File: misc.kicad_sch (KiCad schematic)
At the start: 125 parts, among them CN2 Expansion, CN3 Cartridge, CN5 1P, CN504 AV Out, CN6 1P, IC401 74ACT241, IC513 MC34063AM, IC514 L7805, IC701 PIC16F630/18324, IC901 TL974, J1 Barrel_Jack, J2 EXT, Q1 MMBT3904, U1 TPS564257DRLR, U4 L7805

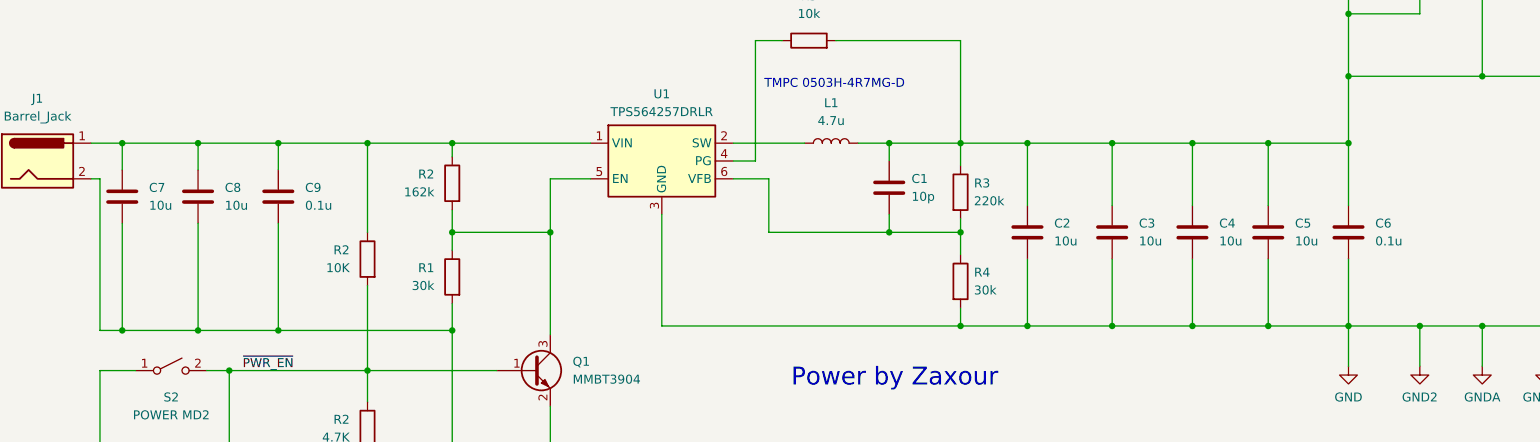
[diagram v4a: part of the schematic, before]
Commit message: BOM/footprint tweaks/corrections.
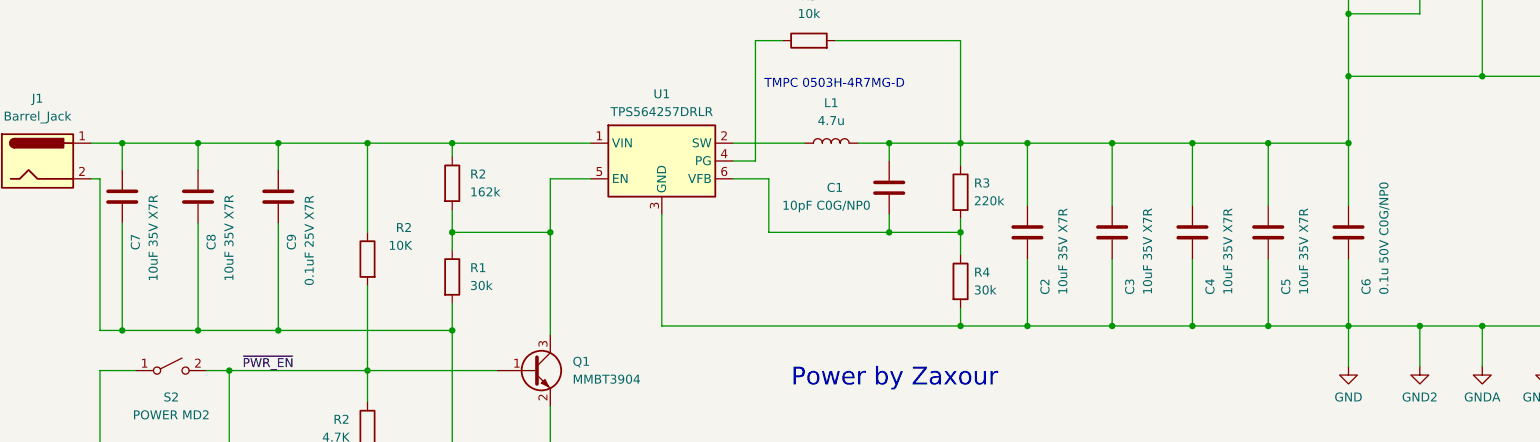
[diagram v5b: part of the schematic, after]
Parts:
- C1: value 10p -> 10pF C0G/NP0
- C2, C3, C4, C5, C7, C8: value 10u -> 10uF 35V X7R
- C6: value 0.1u -> 0.1u 50V C0G/NP0
- C9: value 0.1u -> 0.1uF 25V X7R
- R3, R4, R5: footprint Capacitor_SMD:C_0805_2012Metric -> Resistor_SMD:R_0805_2012Metric
- U1: footprint Package_TO_SOT_SMD:SOT-23-6 -> Neptune:SOT-563
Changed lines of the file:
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@@
       (effects (font (size 1.27 1.27)) (justify left))
     )
-    (property "Footprint" "Capacitor_SMD:C_0805_2012Metric" (at 154.432 227.33 90)
+    (property "Footprint" "Resistor_SMD:R_0805_2012Metric" (at 154.432 227.33 90)
       (effects (font (size 1.27 1.27)) hide)
     )
@@
       (effects (font (size 1.27 1.27)))
     )
-    (property "Footprint" "Package_TO_SOT_SMD:SOT-23-6" (at 114.935 229.235 0)
+    (property "Footprint" "Neptune:SOT-563" (at 114.935 229.235 0)
       (effects (font (size 1.27 1.27)) (justify left) hide)
     )
@@
   )
   (symbol (lib_id "Device:C") (at 146.05 226.695 0) (unit 1)
-    (in_bom yes) (on_board yes) (dnp no) (fields_autoplaced)
-    (property "Reference" "C1" (at 149.225 225.425 0)
+    (in_bom yes) (on_board yes) (dnp no)
+    (property "Reference" "C1" (at 137.16 226.695 0)
       (effects (font (size 1.27 1.27)) (justify left))
     )
-    (property "Value" "10p" (at 149.225 227.965 0)
+    (property "Value" "10pF C0G/NP0" (at 130.81 229.235 0)
       (effects (font (size 1.27 1.27)) (justify left))
     )
@@
   )
   (symbol (lib_id "Device:C") (at 211.455 233.045 0) (unit 1)
-    (in_bom yes) (on_board yes) (dnp no) (fields_autoplaced)
-    (property "Reference" "C6" (at 215.265 231.775 0)
+    (in_bom yes) (on_board yes) (dnp no)
+    (property "Reference" "C6" (at 213.995 241.935 90)
       (effects (font (size 1.27 1.27)) (justify left))
     )
-    (property "Value" "0.1u" (at 215.265 234.315 0)
+    (property "Value" "0.1u 50V C0G/NP0" (at 216.535 241.935 90)
       (effects (font (size 1.27 1.27)) (justify left))
     )
@@
   (symbol (lib_id "Device:C") (at 177.8 233.045 0) (unit 1)
     (in_bom yes) (on_board yes) (dnp no)
-    (property "Reference" "C3" (at 181.61 231.775 0)
+    (property "Reference" "C3" (at 180.34 241.935 90)
       (effects (font (size 1.27 1.27)) (justify left))
     )
-    (property "Value" "10u" (at 181.61 234.315 0)
+    (property "Value" "10uF 35V X7R" (at 182.88 241.935 90)
       (effects (font (size 1.27 1.27)) (justify left))
     )
@@
       (effects (font (size 1.27 1.27)))
     )
-    (property "Footprint" "Capacitor_SMD:C_0805_2012Metric" (at 134.62 207.518 90)
+    (property "Footprint" "Resistor_SMD:R_0805_2012Metric" (at 134.62 207.518 90)
       (effects (font (size 1.27 1.27)) hide)
     )
@@
   (symbol (lib_id "Device:C") (at 47.625 227.965 0) (unit 1)
     (in_bom yes) (on_board yes) (dnp no)
-    (property "Reference" "C8" (at 51.435 226.695 0)
+    (property "Reference" "C8" (at 49.53 235.585 90)
       (effects (font (size 1.27 1.27)) (justify left))
     )
-    (property "Value" "10u" (at 51.435 229.235 0)
+    (property "Value" "10uF 35V X7R" (at 52.07 240.03 90)
       (effects (font (size 1.27 1.27)) (justify left))
     )
@@
     )
   )
-  (symbol (lib_id "Device:R") (at 83.82 239.395 0) (mirror y) (unit 1)
+  (symbol (lib_id "Device:R") (at 83.82 239.395 0) (unit 1)
     (in_bom yes) (on_board yes) (dnp no)
-    (property "Reference" "R1" (at 81.28 238.125 0)
+    (property "Reference" "R1" (at 86.36 238.125 0)
       (effects (font (size 1.27 1.27)) (justify left))
     )
-    (property "Value" "30k" (at 81.28 240.665 0)
+    (property "Value" "30k" (at 86.36 240.665 0)
       (effects (font (size 1.27 1.27)) (justify left))
     )
-    (property "Footprint" "Resistor_SMD:R_0805_2012Metric" (at 85.598 239.395 90)
+    (property "Footprint" "Resistor_SMD:R_0805_2012Metric" (at 82.042 239.395 90)
       (effects (font (size 1.27 1.27)) hide)
     )
@@
       (effects (font (size 1.27 1.27)) (justify left))
     )
-    (property "Footprint" "Capacitor_SMD:C_0805_2012Metric" (at 154.432 240.03 90)
+    (property "Footprint" "Resistor_SMD:R_0805_2012Metric" (at 154.432 240.03 90)
       (effects (font (size 1.27 1.27)) hide)
     )
@@
   (symbol (lib_id "Device:C") (at 189.23 233.045 0) (unit 1)
     (in_bom yes) (on_board yes) (dnp no)
-    (property "Reference" "C4" (at 193.04 231.775 0)
+    (property "Reference" "C4" (at 191.77 241.935 90)
       (effects (font (size 1.27 1.27)) (justify left))
     )
-    (property "Value" "10u" (at 193.04 234.315 0)
+    (property "Value" "10uF 35V X7R" (at 194.31 241.935 90)
       (effects (font (size 1.27 1.27)) (justify left))
     )
@@
   (symbol (lib_id "Device:C") (at 165.735 233.045 0) (unit 1)
     (in_bom yes) (on_board yes) (dnp no)
-    (property "Reference" "C2" (at 169.545 231.775 0)
+    (property "Reference" "C2" (at 168.275 241.935 90)
       (effects (font (size 1.27 1.27)) (justify left))
     )
-    (property "Value" "10u" (at 169.545 234.315 0)
+    (property "Value" "10uF 35V X7R" (at 170.815 241.935 90)
       (effects (font (size 1.27 1.27)) (justify left))
     )
@@
   (symbol (lib_id "Device:R") (at 71.755 236.855 0) (mirror y) (unit 1)
     (in_bom yes) (on_board yes) (dnp no)
-    (property "Reference" "R2" (at 69.215 235.585 0)
+    (property "Reference" "R2" (at 78.105 232.41 0)
       (effects (font (size 1.27 1.27)) (justify left))
     )
-    (property "Value" "10K" (at 69.215 238.125 0)
+    (property "Value" "10K" (at 78.105 234.95 0)
       (effects (font (size 1.27 1.27)) (justify left))
     )
@@
   (symbol (lib_id "Device:C") (at 200.025 233.045 0) (unit 1)
     (in_bom yes) (on_board yes) (dnp no)
-    (property "Reference" "C5" (at 203.835 231.775 0)
+    (property "Reference" "C5" (at 202.565 241.935 90)
       (effects (font (size 1.27 1.27)) (justify left))
     )
-    (property "Value" "10u" (at 203.835 234.315 0)
+    (property "Value" "10uF 35V X7R" (at 205.105 241.935 90)
       (effects (font (size 1.27 1.27)) (justify left))
     )
@@
   (symbol (lib_id "Device:C") (at 36.83 227.965 0) (unit 1)
     (in_bom yes) (on_board yes) (dnp no)
-    (property "Reference" "C7" (at 40.64 226.695 0)
+    (property "Reference" "C7" (at 38.735 235.585 90)
       (effects (font (size 1.27 1.27)) (justify left))
     )
-    (property "Value" "10u" (at 40.64 229.235 0)
+    (property "Value" "10uF 35V X7R" (at 41.275 240.03 90)
       (effects (font (size 1.27 1.27)) (justify left))
     )
@@
   )
   (symbol (lib_id "Device:C") (at 59.055 227.965 0) (unit 1)
-    (in_bom yes) (on_board yes) (dnp no) (fields_autoplaced)
-    (property "Reference" "C9" (at 62.865 226.695 0)
+    (in_bom yes) (on_board yes) (dnp no)
+    (property "Reference" "C9" (at 60.96 235.585 90)
       (effects (font (size 1.27 1.27)) (justify left))
     )
-    (property "Value" "0.1u" (at 62.865 229.235 0)
+    (property "Value" "0.1uF 25V X7R" (at 63.5 240.665 90)
       (effects (font (size 1.27 1.27)) (justify left))
     )
@@
     )
   )
-  (symbol (lib_id "Device:R") (at 83.82 226.06 0) (mirror y) (unit 1)
+  (symbol (lib_id "Device:R") (at 83.82 226.06 0) (unit 1)
     (in_bom yes) (on_board yes) (dnp no)
-    (property "Reference" "R2" (at 81.28 224.79 0)
+    (property "Reference" "R2" (at 86.36 224.79 0)
       (effects (font (size 1.27 1.27)) (justify left))
     )
-    (property "Value" "162k" (at 81.28 227.33 0)
+    (property "Value" "162k" (at 86.36 227.33 0)
       (effects (font (size 1.27 1.27)) (justify left))
     )
-    (property "Footprint" "Resistor_SMD:R_0805_2012Metric" (at 85.598 226.06 90)
+    (property "Footprint" "Resistor_SMD:R_0805_2012Metric" (at 82.042 226.06 90)
       (effects (font (size 1.27 1.27)) hide)
     )

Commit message: Misc. tweaks/improvements.
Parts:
- removed C1, C35, C583, C584: 100nF, Capacitor_SMD:C_0805_2012Metric, symbol Device:C
- removed C585: 470pF, Capacitor_SMD:C_0805_2012Metric, symbol Device:C
- removed CE16: 220uF/16V, Capacitor_THT:CP_Radial_D8.0mm_P5.00mm, symbol Device:C_Polarized
- removed CE17, CE519: 100uF, Capacitor_THT:CP_Radial_D5.0mm_P2.50mm, symbol Device:C_Polarized
- removed CE18, CE19: 47uF, Capacitor_THT:CP_Radial_D5.0mm_P2.50mm, symbol Device:C_Polarized
- removed CE516: 220uF, Capacitor_THT:CP_Radial_D5.0mm_P2.50mm, symbol Device:C_Polarized
- removed CF1: ~, symbol Device:Filter_EMI_CommonMode
- removed D2, D501: D, symbol Device:D
- removed IC513: MC34063AM, Package_SO:SOIC-8_3.9x4.9mm_P1.27mm, symbol Regulator_Switching:MC34063AD
- removed IC514, U4: L7805, symbol Regulator_Linear:L7805
- removed JX1: Barrel_Jack, Neptune:Power_Jack, symbol Connector:Barrel_Jack
- removed L507: 330uH/100uH, Inductor_SMD:L_0805_2012Metric, symbol Device:L
- removed L6: 100uH, Inductor_SMD:L_0805_2012Metric, symbol Device:L
- removed R550: 0.13, Resistor_SMD:R_0805_2012Metric, symbol Device:R
- removed R551: 560, Resistor_SMD:R_0805_2012Metric, symbol Device:R
- removed R552: 220, Resistor_SMD:R_0805_2012Metric, symbol Device:R
- removed R553, R555: 10K, Resistor_SMD:R_0805_2012Metric, symbol Device:R
- removed R554: 3.3K, Resistor_SMD:R_0805_2012Metric, symbol Device:R
- removed R556: 4.7K, Resistor_SMD:R_0805_2012Metric, symbol Device:R
- removed R557: 1K, Resistor_SMD:R_0805_2012Metric, symbol Device:R
- removed RX500: 11.8K, symbol Device:R
- removed SX2: POWER, Neptune:Power_Switch, symbol Switch:SW_SPST
- removed TR503, TR504: NPN, symbol Simulation_SPICE:NPN
- removed TR505: ~, symbol 32X:FX401
- added D801: 3A RECT, Diode_SMD:D_SOD-128, symbol Device:D
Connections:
- net at C7.1, C8.1, C9.1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: now also D801.1 (K); no longer J1.1
- new net: D801.2 (A), J1.1
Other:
- note removed: "32X power"
- note removed: "CF1 is shared between MD2 and 32X. Is this rated for the required current?"
- note removed: "Install RX500 if IC513 is NCP3063/NCV3063"
- note removed: "L507 value 100uH if IC513 is NCP3063/NCV3063"
- note removed: "Mega Drive power"
- moved on the sheet: C7, C8, C9, CE517, CE518, R2
